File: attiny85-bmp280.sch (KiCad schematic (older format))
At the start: 11 parts, among them J1 5.5V, J2 GND, J3 3.3V, J4 SCL, J5 SDA, J6 GND, U1 AMS1117-3.3, U2 ATtiny85-20PU

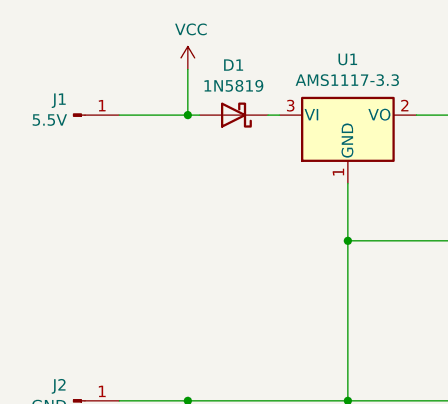
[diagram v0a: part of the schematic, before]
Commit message: Correct input voltage.
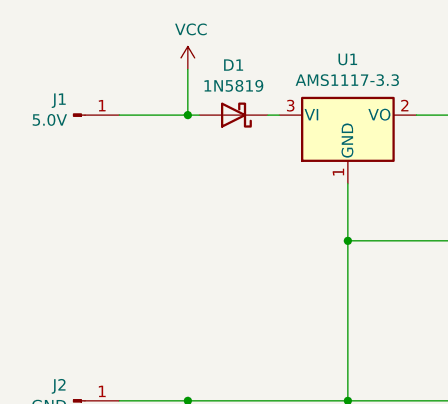
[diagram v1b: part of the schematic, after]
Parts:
- J1: value 5.5V -> 5.0V
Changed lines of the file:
@@
 P 2550 3050
 F 0 "J1" H 2522 2982 50  0000 R CNN
-F 1 "5.5V" H 2522 3073 50  0000 R CNN
+F 1 "5.0V" H 2522 3073 50  0000 R CNN
 F 2 "" H 2550 3050 50  0001 C CNN
 F 3 "~" H 2550 3050 50  0001 C CNN
